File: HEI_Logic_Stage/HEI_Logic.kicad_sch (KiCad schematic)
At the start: 89 parts, among them J3 RJ_{1}, J4 Conn_02x10_Odd_Even, J4 RJ_{2}, J5 430450813_Molex, J5 Tag-Connect, SW1 SW_Push, SW4 SW_SPST, U10 B1203XT-1WR3, U11 ADM3058EBRIZ, U6 STM32F334C8T6, U7 LM4132-Q1 SOT-2, U8 5V_Converter_R-78E5.0-0.5

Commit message: logic stage motor interface schematic
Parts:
- added U7: CD40109BQNSRQ1, CD40109BQNSRQ1:SOIC127P780X200-16N, symbol CD40109B-Q1:CD40109BQNSRQ1
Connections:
- net GND: now also U7.15 (EN_D), U7.8 (VSS)
- net HallIN1: now also U7.3 (A); no longer U6.10 (PA0)
- net HallIN2: now also U7.6 (B); no longer U6.11 (PA1)
- net HallIN3: now also U7.10 (C); no longer U6.18 (PB0)
- net V_Hall: now also U7.16 (VDD)
- new net: U7.1 (VCC), U7.2 (EN_A), U7.7 (EN_B), U7.9 (EN_C)
- new net HallIN1_3v3: U6.10 (PA0), U7.4 (E)
- new net HallIN2_3v3: U6.11 (PA1), U7.5 (F)
- new net HallIN3_3v3: U6.18 (PB0), U7.11 (G)
- no-connect marks 11 -> 13
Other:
- note added: "12 or 5 V => 3.3V Hall Inputs TODO: Check symbol and pinout"
- note added: "CAN Power & Transceiver"
- note added: "GND Reference for Thermistor and Hall"
- note added: "Hall inputs: GPIO-bound Thermistor Input: ADC-bound"
- note added: "High Efficiency Inverter Logic Stage"
- note added: "Microcontroller"
- note added: "Motor Interface"
- note added: "Power Converters"
- note added: "Power Stage Connector"
- note added: "Tag-Connect (SWD & UART)"
- note removed: "CAN"
- note removed: "UART / SWD"
- note removed: "to Power Stage"
- moved on the sheet: C33, C35, C36, C37, C39, C40, C42, C43, C45, C47, C48, C49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

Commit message: layouted updated HEI-Logic
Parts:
- removed R66: 10k, Resistor_SMD:R_0603_1608Metric_Pad0.98x0.95mm_HandSolder, symbol Device:R_US
- added C42 (x2): 1uF, Capacitor_SMD:C_0603_1608Metric_Pad1.08x0.95mm_HandSolder, symbol Device:C
- added JP4, JP5: Jumper_2_Open, Jumper:SolderJumper-2_P1.3mm_Open_RoundedPad1.0x1.5mm, symbol Jumper:Jumper_2_Open
- added R61: 10k, Resistor_SMD:R_0603_1608Metric_Pad0.98x0.95mm_HandSolder, symbol Device:R_Small_US
- added R66 (x3): X, Resistor_SMD:R_0603_1608Metric_Pad0.98x0.95mm_HandSolder, symbol Device:R_US
- added U8: TMH 1212S, GTSR_KiCAD_Footprints:TMH SINGLE_TRP, symbol TMH1212S:TMH_1212S
- JP1: footprint (none) -> Jumper:SolderJumper-3_P1.3mm_Open_RoundedPad1.0x1.5mm_NumberLabels
- R66: value 10k -> X
- U7: footprint CD40109BQNSRQ1:SOIC127P780X200-16N -> GTSR_KiCAD_Footprints:SOIC127P780X200-16N
- U8: now not fitted
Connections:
- net +3V3: now also U7.16 (VDD); no longer R66.1
- net 12V_LV: now also C42.1, U8.1 (+VIN(VCC))
- net 12V_MCU: now also TP23.1, C42.1, U8.6 (+VOUT)
- net GND: now also J4.16 (Pin_16), C42.2, R61.1, U8.4 (-VOUT)
- net GND_LV: now also C42.2, U8.2 (-VIN(GND))
- net HallIN3: now also J5.7; no longer J5.6
- net HallIN3_3v3: now also U6.14 (PA4); no longer U6.18 (PB0)
- net TIN1: now also J5.3, U6.18 (PB0), R66.2; no longer J5.4, R66.2, U6.19 (PB1)
- net V_Hall: now also U7.1 (VCC), U7.2 (EN_A), U7.7 (EN_B), U7.9 (EN_C); no longer U7.16 (VDD)
- net Vref: now also R66.1, R66.1, R66.1, R66.1
- net 10kSaver: now reaches U6.44 (PH3-BOOT0)
- net 10kSaver: now also U6.3 (PC14-OSC32_IN), U6.4 (PC15-OSC32_OUT), U6.5 (PH0-OSC_IN), U6.6 (PH1-OSC_OUT), R61.2
- net HallIN1 renamed HallIN1/TIN3
- net HallIN1/TIN3: now also JP4.2 (B), R66.2
- net HallIN1_3v3 renamed HallIN1_3v3/ADC
- net HallIN1_3v3/ADC: now also JP4.1 (A)
- net HallIN2 renamed HallIN2/TIN4
- net HallIN2/TIN4: now also J5.6, JP5.2 (B), R66.2; no longer J5.3
- net HallIN2_3v3 renamed HallIN2_3v3/ADC
- net HallIN2_3v3/ADC: now also JP5.1 (A)
- net I2C_SCL: no longer names the net of U6.42 (PB6)
- net I2C_SDA: no longer names the net of U6.43 (PB7)
- new net TIN2: J5.4, R66.2, U6.19 (PB1)
- no-connect marks 13 -> 9
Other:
- note added: "12 (Car LV) -ISO> 12 (MCU) TMA1212S (1W) or TMH1212S (2W)"
- note added: "CAN Transceiver & RJ45s"
- note added: "Do not populate 5V converter if selecting 12V"
- note added: "HallIN1-2 may also be used as thermistor inputs if pull-ups are soldered in, U7 is removed, and the jumpers are soldered in. (HallIN3 will be unusable)"
- note added: "Microcontroller Region"
- note added: "TODO: Select smaller 5 V supply (lower current requirement)"
- note added: "Thermistor Pull-ups"
- note removed: "12 (Car LV) -ISO> 12 (MCU)"
- note removed: "CAN Power & Transceiver"
- note removed: "Microcontroller"
- note removed: "Thermistor Pull-up"
- moved on the sheet: C42, C43, C48, C49, H2, J3, J4, J5, JP1, R66, R70, R71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

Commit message: initial edits to logic stage schematic
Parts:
- added J6: Conn_02x10_Odd_Even, Connector_PinSocket_2.54mm:PinSocket_2x10_P2.54mm_Horizontal, symbol Connector_Generic:Conn_02x10_Odd_Even
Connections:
- net 12V_LV: no longer J4.19 (Pin_19)
- net GND: now also J4.20 (Pin_20), J6.20 (Pin_20); no longer J4.16 (Pin_16), J4.17 (Pin_17)
- net GND_LV: no longer J4.20 (Pin_20)
- net 12V_MCU renamed +12V_MCU
- net +12V_MCU: now also J4.19 (Pin_19)
- net 5V_CAN renamed +5V_CAN
- net 5V_MCU renamed +5V
- net +5V: now also J6.18 (Pin_18)
- new net DCIsense+: J6.13 (Pin_13)
- new net DCIsense-: J6.15 (Pin_15)
- new net DCVsense+: J6.17 (Pin_17)
- new net DCVsense-: J6.19 (Pin_19)
- new net PhA_Isense+: J6.1 (Pin_1)
- new net PhA_Isense-: J6.3 (Pin_3)
- new net PhB_Isense+: J6.5 (Pin_5)
- new net PhB_Isense-: J6.7 (Pin_7)
- new net PhC_Isense+: J6.9 (Pin_9)
- new net PhC_Isense-: J6.11 (Pin_11)
- no-connect marks 9 -> 11
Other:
- note added: "CONTROLS/COMMS"
- note added: "If using differential signalling, select a diff. amp to use here"
- note added: "MCU Options: - TI C2000 Series - STM - RP2040 (ADC limitation)"
- note added: "Need to find MCU with enough available ADC channels (Minimum 3xIphase, 1xVbus; optional 1xIbus, thermistors)"
- note added: "Power Stage Connectors"
- note added: "SENSING"
- note added: "thermistor inputs?"
- note removed: "Power Stage Connector"
- moved on the sheet: H2, J4

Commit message: major logic stage updates
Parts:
- removed C42 (x2): 1uF, Capacitor_SMD:C_0603_1608Metric_Pad1.08x0.95mm_HandSolder, symbol Device:C
- removed C42 (x2), C43 (x2), C47: 10uF, Capacitor_SMD:C_0603_1608Metric_Pad1.08x0.95mm_HandSolder, symbol Device:C
- removed C45: 2.2uF, Capacitor_SMD:C_0603_1608Metric_Pad1.08x0.95mm_HandSolder, symbol Device:C
- removed C48, C49: 0.1uF, Capacitor_SMD:C_0603_1608Metric_Pad1.08x0.95mm_HandSolder, symbol Device:C_Small
- removed D13: 12V_TVS_ESD12VD3B-TP, GTSR_KiCAD_Footprints:ESD12VD3B-TP, symbol GTSR_symbol_lib:12V_TVS_ESD12VD3B-TP
- removed J3: RJ_{1}, GTSR_KiCAD_Footprints:ASSMANN_A-2004-2-4-LPS-N-R, symbol Connector:8P8C_Shielded
- removed J4, J6: Conn_02x10_Odd_Even, Connector_PinSocket_2.54mm:PinSocket_2x10_P2.54mm_Horizontal, symbol Connector_Generic:Conn_02x10_Odd_Even
- removed J4: RJ_{2}, GTSR_KiCAD_Footprints:ASSMANN_A-2004-2-4-LPS-N-R, symbol Connector:8P8C_Shielded
- removed J5: 430450813_Molex, Connector_Molex:Molex_Micro-Fit_3.0_43045-0812_2x04_P3.00mm_Vertical, symbol GTSR_symbol_lib:2068320801_Molex
- removed JP1: Jumper_3_Open, Jumper:SolderJumper-3_P1.3mm_Open_RoundedPad1.0x1.5mm_NumberLabels, symbol Jumper:Jumper_3_Open
- removed JP4, JP5: Jumper_2_Open, Jumper:SolderJumper-2_P1.3mm_Open_RoundedPad1.0x1.5mm, symbol Jumper:Jumper_2_Open
- removed R61 (x8): 330, Resistor_SMD:R_0603_1608Metric_Pad0.98x0.95mm_HandSolder, symbol Device:R_Small_US
- removed R66 (x4): X, Resistor_SMD:R_0603_1608Metric_Pad0.98x0.95mm_HandSolder, symbol Device:R_US
- removed R70: 120, Resistor_SMD:R_0603_1608Metric_Pad0.98x0.95mm_HandSolder, symbol Device:R_Small_US
- removed SW4: SW_SPST, GTSR_KiCAD_Footprints:SW_DS04-254-1-01BK-SMT, symbol Switch:SW_SPST
- removed TP23 (x22): Test_Point, TestPoint:TestPoint_Pad_D1.0mm, symbol GTSR_symbol_lib:Test_Point
- removed U10: B1203XT-1WR3, GTSR_KiCAD_Footprints:B_XT-1WR3_MNS-M, symbol GTSR_symbol_lib:B1203XT-1WR3
- removed U11: ADM3058EBRIZ, GTSR_KiCAD_Footprints:8-SOIC_ADM3058EBRIZ, symbol GTSR_symbol_lib:CAN_Trans_ADM3058EBRIZ
- removed U7: CD40109BQNSRQ1, GTSR_KiCAD_Footprints:SOIC127P780X200-16N, symbol CD40109B-Q1:CD40109BQNSRQ1
- removed U8 (x2): 5V_Converter_R-78E5.0-0.5, GTSR_KiCAD_Footprints:R-78E5.0-0.5, symbol GTSR_symbol_lib:5V_Converter_R-78E5.0-0.5
- removed U8: TMH 1212S, GTSR_KiCAD_Footprints:TMH SINGLE_TRP, symbol TMH1212S:TMH_1212S
- added D12, D13, D14, D15, D16, D17, D18, D8: 3v3, Diode_SMD:D_SOD-923, symbol Diode:ESD9B3.3ST5G
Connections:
- net MISO is gone; now on net TIN1: U6.16 (PA6)
- net MOSI_r is gone; now on net TIN2: U6.17 (PA7)
- net ~{CS2}_r is gone; now on net HallIN3_3v3: U6.21 (PB10)
- net GND: now also D12.2 (A2), D13.2 (A2), D14.2 (A2), D15.2 (A2), D16.2 (A2), D17.2 (A2), D18.2 (A2), D8.2 (A2)
- net HallIN3_3v3: no longer U6.14 (PA4)
- net TIN1: now also D8.1 (A1); no longer U6.18 (PB0)
- net TIN2: now also D12.1 (A1); no longer U6.19 (PB1)
- net UART_RX: now also U6.43 (PB7); no longer U6.13 (PA3)
- net UART_TX: now also U6.42 (PB6); no longer U6.12 (PA2)
- net 10kSaver renamed Unused
- net HRTIM_C1_r: no longer names the net of U6.25 (PB12)
- net HRTIM_C2_r: no longer names the net of U6.26 (PB13)
- net HallIN1_3v3/ADC renamed PhA_I
- net PhA_I: now also D17.1 (A1)
- net HallIN2_3v3/ADC renamed PhB_I
- net PhB_I: now also D14.1 (A1)
- net SCK_r renamed DCV
- net DCV: now also D18.1 (A1)
- net ~{CS1}_r renamed TIN3
- net TIN3: now also D13.1 (A1)
- net ~{CS3}_r: no longer names the net of U6.22 (PB11)
- net ~{CS4}_r: no longer names the net of U6.38 (PA15)
- new net DCI: D16.1 (A1), U6.14 (PA4)
- new net HallIN1_3v3: U6.18 (PB0)
- new net HallIN2_3v3: U6.19 (PB1)
- new net PhC_I: D15.1 (A1), U6.12 (PA2)
- no-connect marks 11 -> 10
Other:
- added sheet Control & Motor Interface (HEI_Logic_INTERFACE.kicad_sch)
- added sheet Power & CAN (HEI_Logic_PWRCAN.kicad_sch)
- note added: "Hierarchy"
- note added: "MCU Zone"
- note added: "Sensing 3v3 clamp diodes (low capacitance)"
- note added: "TODOs: - Select 5V_MCU supply - Add bypass caps to all ICs that recommend it - Update parts folder"
- note removed: "12 (Car LV) -> 5 (CAN)"
- note removed: "12 (Car LV) -ISO> 12 (MCU) TMA1212S (1W) or TMH1212S (2W)"
- note removed: "12 (Car LV) -ISO> 3V3 (Digital)"
- note removed: "12 (MCU) -> 5 (MCU)"
- note removed: "12 or 5 V => 3.3V Hall Inputs TODO: Check symbol and pinout"
- note removed: "CAN Transceiver & RJ45s"
- note removed: "CONTROLS/COMMS"
- note removed: "Do not populate 5V converter if selecting 12V"
- note removed: "GND Reference for Thermistor and Hall"
- note removed: "Hall inputs: GPIO-bound Thermistor Input: ADC-bound"
- note removed: "HallIN1-2 may also be used as thermistor inputs if pull-ups are soldered in, U7 is removed, and the jumpers are soldered in. (HallIN3 will be unusable)"
- note removed: "If using differential signalling, select a diff. amp to use here"
- note removed: "MCU Options: - TI C2000 Series - STM - RP2040 (ADC limitation)"
- note removed: "Microcontroller Region"
- note removed: "Motor Interface"
- note removed: "Need to find MCU with enough available ADC channels (Minimum 3xIphase, 1xVbus; optional 1xIbus, thermistors)"
- note removed: "Power Converters"
- note removed: "Power Stage Connectors"
- note removed: "SENSING"
- note removed: "TODO: Select smaller 5 V supply (lower current requirement)"
- note removed: "Thermistor Pull-ups"
- note removed: "thermistor inputs?"
- note removed: "to Motor"
- moved on the sheet: C33, C35, C36, C37, C39, C40, D10, D11, D14, D9, H2, J5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

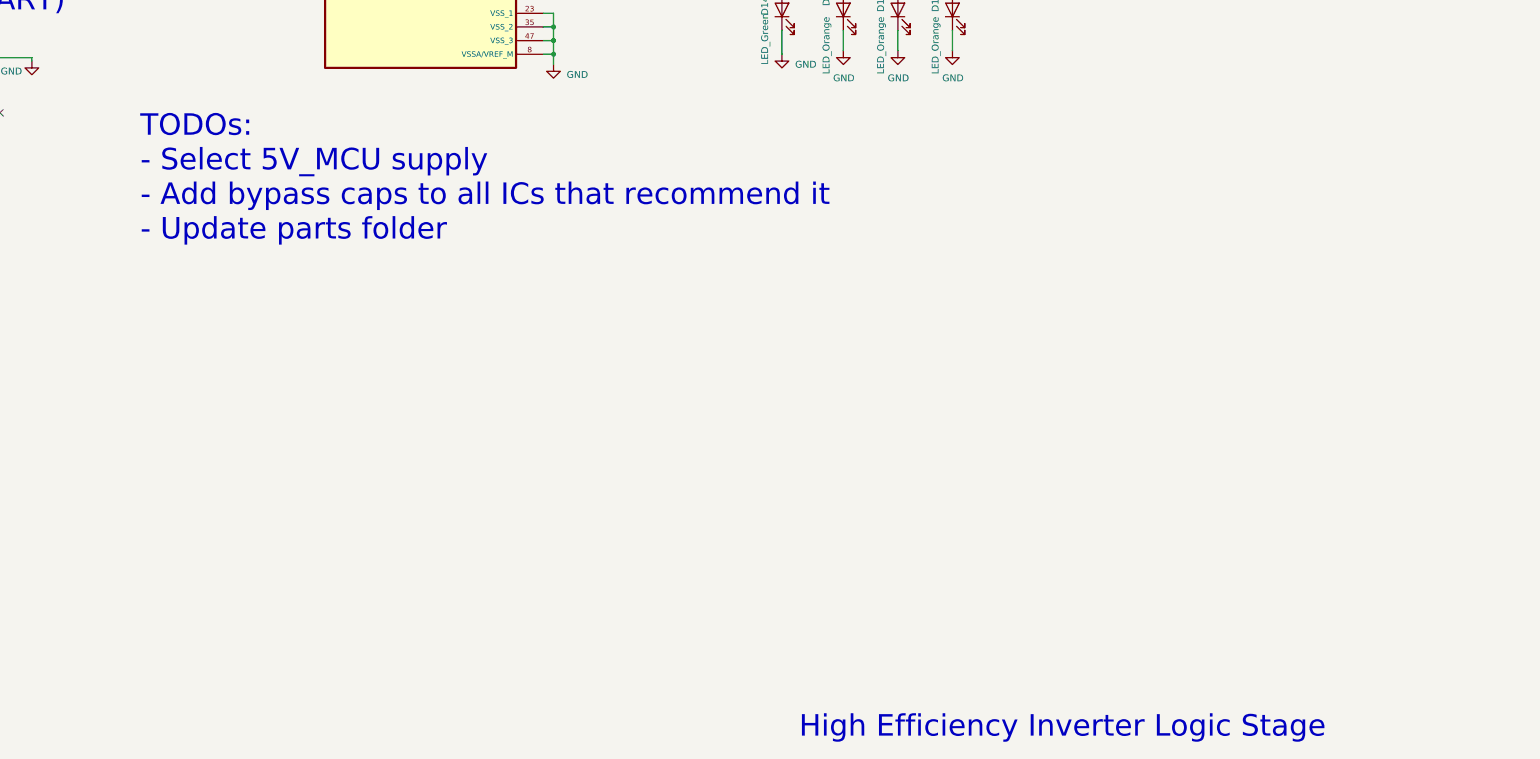
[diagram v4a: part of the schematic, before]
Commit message: new parts into Parts
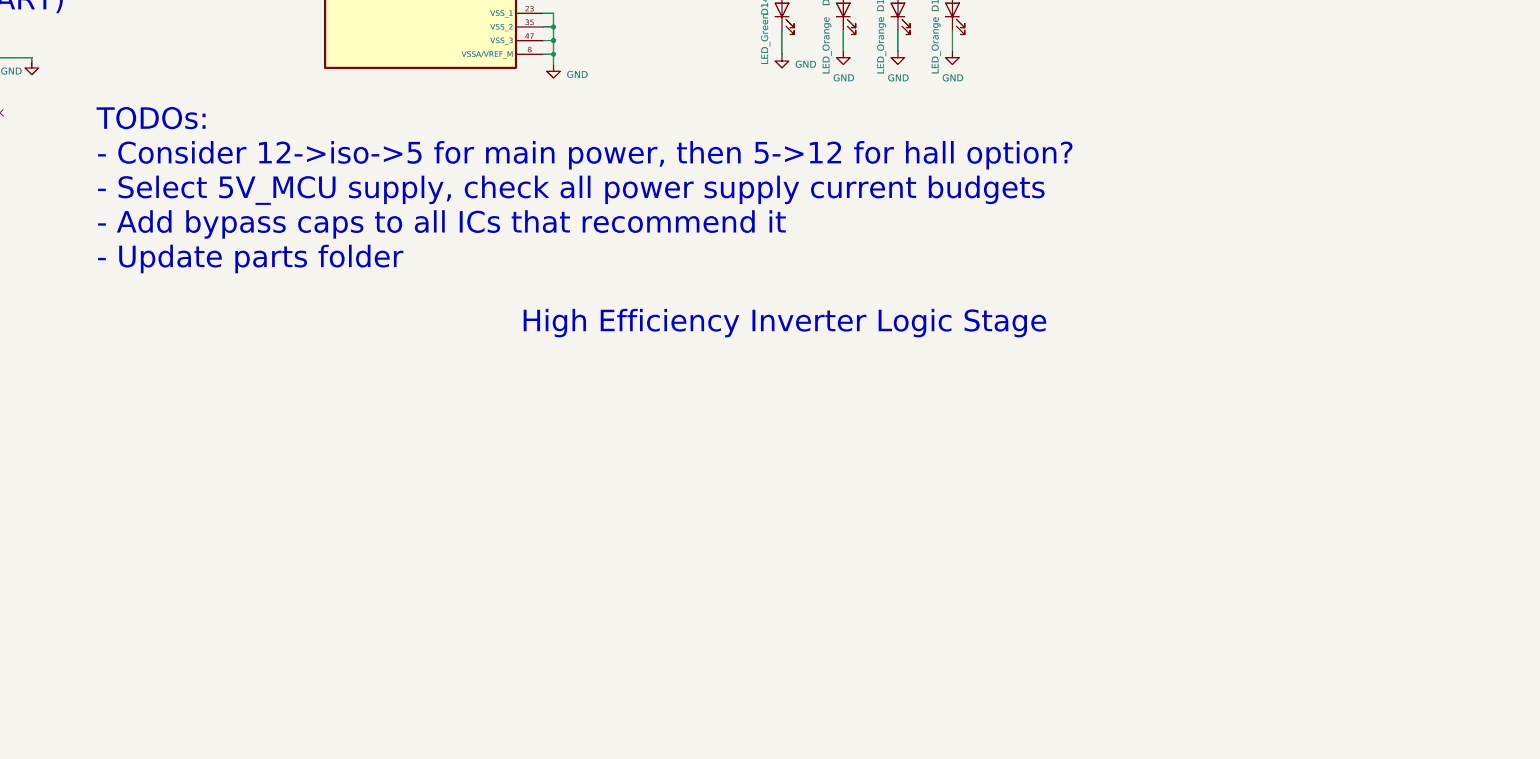
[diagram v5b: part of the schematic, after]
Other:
- note added: "TODOs: - Consider 12->iso->5 for main power, then 5->12 for hall option? - Select 5V_MCU supply, check all power supply current budgets - Add bypass caps to all ICs that recommend it - Update parts folder"
- note removed: "TODOs: - Select 5V_MCU supply - Add bypass caps to all ICs that recommend it - Update parts folder"
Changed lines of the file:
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@@
 	(text "High Efficiency Inverter Logic Stage"
 		(exclude_from_sim no)
-		(at 232.41 252.095 0)
-		(effects
-			(font
-				(face "Tahoma")
+		(at 180.594 176.784 0)
+		(effects
+			(font
+				(face "Rockwell")
 				(size 4 4)
 			)
@@
 		)
 	)
-	(text "TODOs:\n- Select 5V_MCU supply\n- Add bypass caps to all ICs that recommend it\n- Update parts folder"
+	(text "TODOs:\n- Consider 12->iso->5 for main power, then 5->12 for hall option?\n- Select 5V_MCU supply, check all power supply current budgets\n- Add bypass caps to all ICs that recommend it\n- Update parts folder"
 		(exclude_from_sim no)
-		(at 109.728 159.512 0)
+		(at 101.6 164.846 0)
 		(effects
 			(font
@@
 	(label "TIN1"
 		(at 86.106 59.69 0)
+		(fields_autoplaced yes)
 		(effects
 			(font
@@
 	(label "TIN2"
 		(at 86.106 62.23 0)
+		(fields_autoplaced yes)
 		(effects
 			(font
@@
 	(label "CAN_TX"
 		(at 49.53 52.07 0)
+		(fields_autoplaced yes)
 		(effects
 			(font
@@
 	(label "HallIN1_3v3"
 		(at 86.106 52.07 0)
+		(fields_autoplaced yes)
 		(effects
 			(font
@@
 	(label "PhB_I"
 		(at 86.106 37.973 0)
+		(fields_autoplaced yes)
 		(effects
 			(font
@@
 	(label "CAN_RX"
 		(at 49.53 54.61 0)
+		(fields_autoplaced yes)
 		(effects
 			(font
@@
 	(label "PhC_I"
 		(at 86.106 40.513 0)
+		(fields_autoplaced yes)
 		(effects
 			(font
@@
 	(label "DCI"
 		(at 86.106 43.053 0)
+		(fields_autoplaced yes)
 		(effects
 			(font
@@
 	(label "HallIN2_3v3"
 		(at 86.106 54.61 0)
+		(fields_autoplaced yes)
 		(effects
 			(font
@@
 	(label "TIN3"
 		(at 86.106 64.77 0)
+		(fields_autoplaced yes)
 		(effects
 			(font
@@
 	(label "PhA_I"
 		(at 86.106 35.433 0)
+		(fields_autoplaced yes)
 		(effects
 			(font
@@
 	(label "HallIN3_3v3"
 		(at 86.106 57.15 0)
+		(fields_autoplaced yes)
 		(effects
 			(font
@@
 	(label "DCV"
 		(at 86.106 45.593 0)
-		(effects
-			(font
+		(fields_autoplaced yes)
+		(effects
+			(font

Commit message: more minor updates
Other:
- note added: "TODOs: - Consider 12->iso->5 for main power, then 5->12 for hall option? - Select 5V_MCU supply, check all power supply current budgets"
- note removed: "TODOs: - Consider 12->iso->5 for main power, then 5->12 for hall option? - Select 5V_MCU supply, check all power supply current budgets - Add bypass caps to all ICs that recommend it - Update parts folder"
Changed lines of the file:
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@@
 		)
 	)
-	(text "TODOs:\n- Consider 12->iso->5 for main power, then 5->12 for hall option?\n- Select 5V_MCU supply, check all power supply current budgets\n- Add bypass caps to all ICs that recommend it\n- Update parts folder"
+	(text "TODOs:\n- Consider 12->iso->5 for main power, then 5->12 for hall option?\n- Select 5V_MCU supply, check all power supply current budgets"
 		(exclude_from_sim no)
 		(at 101.6 164.846 0)
